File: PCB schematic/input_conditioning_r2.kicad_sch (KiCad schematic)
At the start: 11 parts, among them J1 Conn_Coaxial, J2 Conn_Coaxial, J3 Conn_01x02_Socket, J4 Conn_01x02_Socket

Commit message: schematic
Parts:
- removed J1, J2: Conn_Coaxial, symbol Connector:Conn_Coaxial
- removed J3: Conn_01x02_Socket, symbol Connector:Conn_01x02_Socket
- added J3: Conn_Coaxial_x2, Misc. Footprints:CONN_6575_AMP, symbol Connector:Conn_Coaxial_x2
- C19: footprint Capacitor_THT:C_Radial_D5.0mm_H11.0mm_P2.00mm -> Capacitor_THT:CP_Radial_D5.0mm_P2.50mm
- J4: footprint (none) -> Connector_PinSocket_2.54mm:PinSocket_1x02_P2.54mm_Vertical
- R1, R2, R3: footprint (none) -> Resistor_SMD:R_0603_1608Metric_Pad0.98x0.95mm_HandSolder
- V1: now left out of the parts list
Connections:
- net GND: now also J3.3 (EXT)
- net input_1: now also J3.1 (IN1)
- net input_2: now also J3.2 (IN2)
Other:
- added sheet User Interface (../Oscilloscope User Interface/Oscilloscope User Interface.kicad_sch)

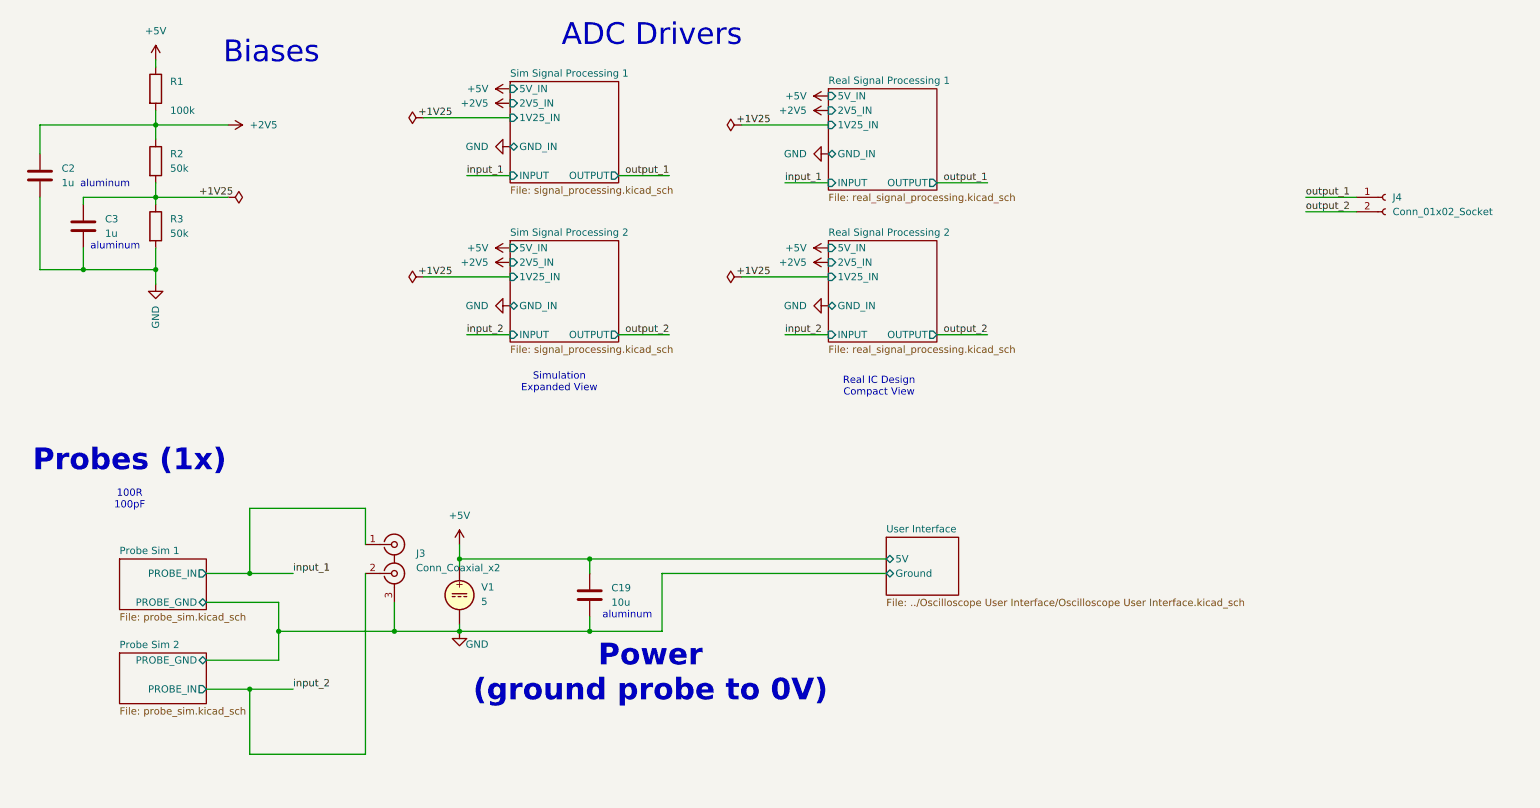
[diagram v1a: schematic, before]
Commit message: schematic layout mostly done
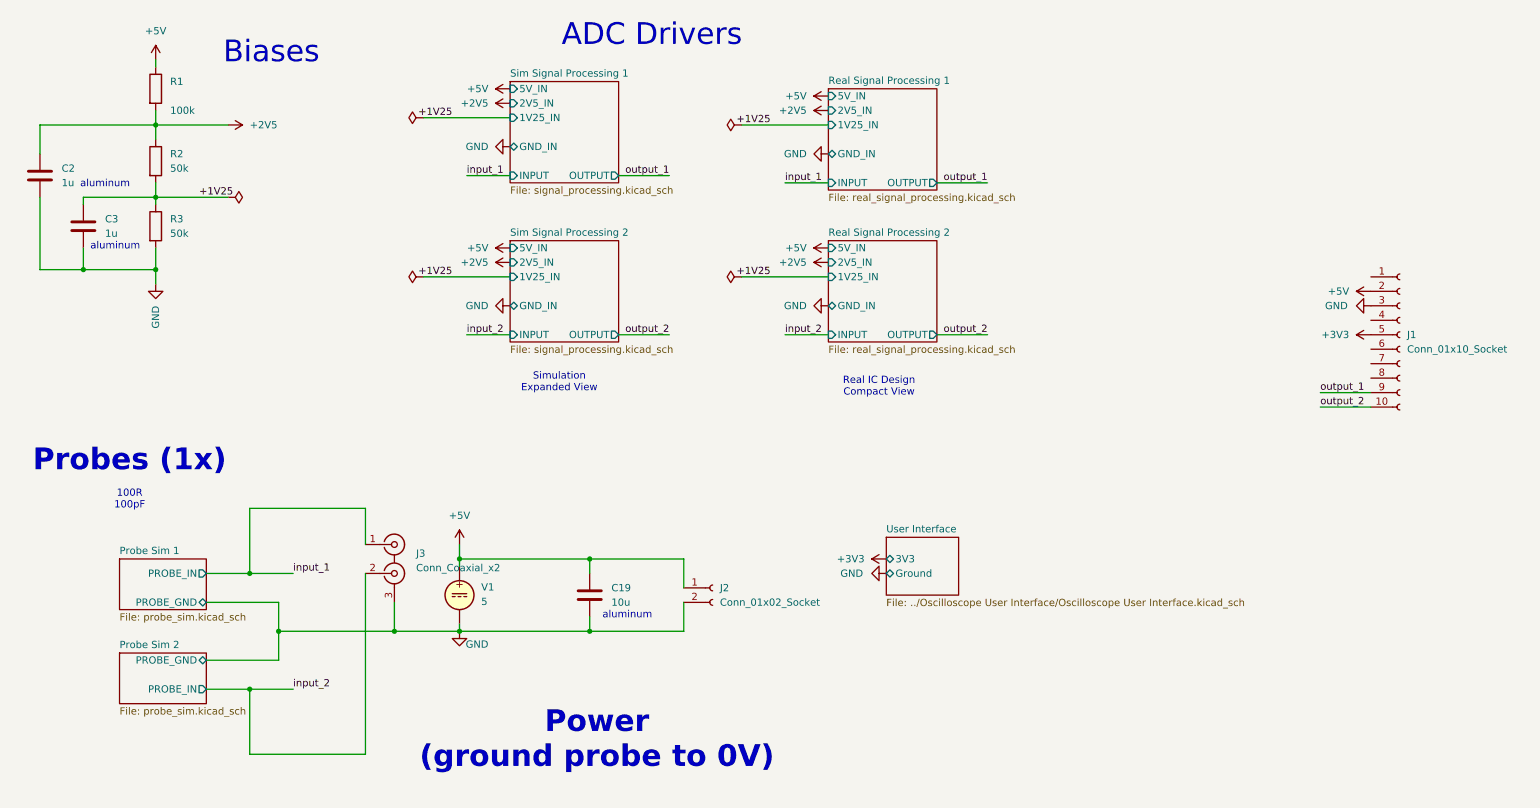
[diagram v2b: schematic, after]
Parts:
- removed J4: Conn_01x02_Socket, Connector_PinSocket_2.54mm:PinSocket_1x02_P2.54mm_Vertical, symbol Connector:Conn_01x02_Socket
- added J1: Conn_01x10_Socket, Connector_PinSocket_2.54mm:PinSocket_1x10_P2.54mm_Vertical, symbol Connector:Conn_01x10_Socket
- added J2: Conn_01x02_Socket, Connector_PinSocket_2.00mm:PinSocket_1x02_P2.00mm_Vertical, symbol Connector:Conn_01x02_Socket
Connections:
- net +5V: now also J1.2 (Pin_2), J2.1 (Pin_1)
- net GND: now also J1.3 (Pin_3), J2.2 (Pin_2)
- net output_1: now also J1.9 (Pin_9)
- net output_2: now also J1.10 (Pin_10)
- new net +3V3: J1.5 (Pin_5)
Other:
- sheet User Interface ports: added 3V3; removed 5V

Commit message: pcb initial complete revision
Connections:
- net output_1: now also J1.10 (Pin_10); no longer J1.9 (Pin_9)
- net output_2: now also J1.9 (Pin_9); no longer J1.10 (Pin_10)
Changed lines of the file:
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@@
 	(wire
 		(pts
+			(xy 242.57 85.09) (xy 251.46 85.09)
+		)
+		(stroke
+			(width 0)
+			(type default)
+		)
+	)
+	(wire
+		(pts
 			(xy 114.3 114.3) (xy 114.3 116.84)
 		)
@@
 	(wire
 		(pts
-			(xy 242.57 85.09) (xy 251.46 85.09)
+			(xy 54.61 137.16) (xy 54.61 148.59)
 		)
 		(stroke
@@
 	(wire
 		(pts
-			(xy 54.61 137.16) (xy 54.61 148.59)
+			(xy 242.57 87.63) (xy 251.46 87.63)
 		)
 		(stroke
@@
 	(wire
 		(pts
-			(xy 242.57 87.63) (xy 251.46 87.63)
-		)
-		(stroke
-			(width 0)
-			(type default)
-		)
-	)
-	(wire
-		(pts
 			(xy 92.71 46.99) (xy 100.33 46.99)
 		)
@@
 	)
 	(label "output_1"
-		(at 242.57 85.09 0)
+		(at 242.57 87.63 0)
 		(effects
 			(font
@@
 	)
 	(label "output_2"
-		(at 242.57 87.63 0)
+		(at 242.57 85.09 0)
 		(effects
 			(font
@@
 		(unit 1)
 		(body_style 1)
-		(exclude_from_sim no)
+		(exclude_from_sim yes)
 		(in_bom yes)
 		(on_board yes)
@@
 			)
 		)
-		(pin "3V3" bidirectional
+		(pin "3V3" input
 			(at 166.37 114.3 180)
 			(effects
